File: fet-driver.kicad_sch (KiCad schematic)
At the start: 32 parts, among them Q21 AO3401, Q22 AO3401, Q23 AO3401, Q24 AO3401, Q25 AO3401, Q26 AO3401, Q27 AO3401, Q28 AO3401

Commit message: KiCAD ver. up
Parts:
- renumbered C47 to C39, C48 to C40, C49 to C41, C50 to C42, C51 to C43, C52 to C44, C53 to C45, C54 to C46, Q21 to Q13, Q22 to Q14, Q23 to Q15, Q24 to Q16, Q25 to Q17, Q26 to Q18, Q27 to Q19, Q28 to Q20, R90 to R66, R91 to R67, R92 to R68, R93 to R69, R94 to R70, R95 to R71, R96 to R72, R97 to R73, R106 to R82, R107 to R83, R108 to R84, R109 to R85, R110 to R86, R111 to R87, R112 to R88, R113 to R89

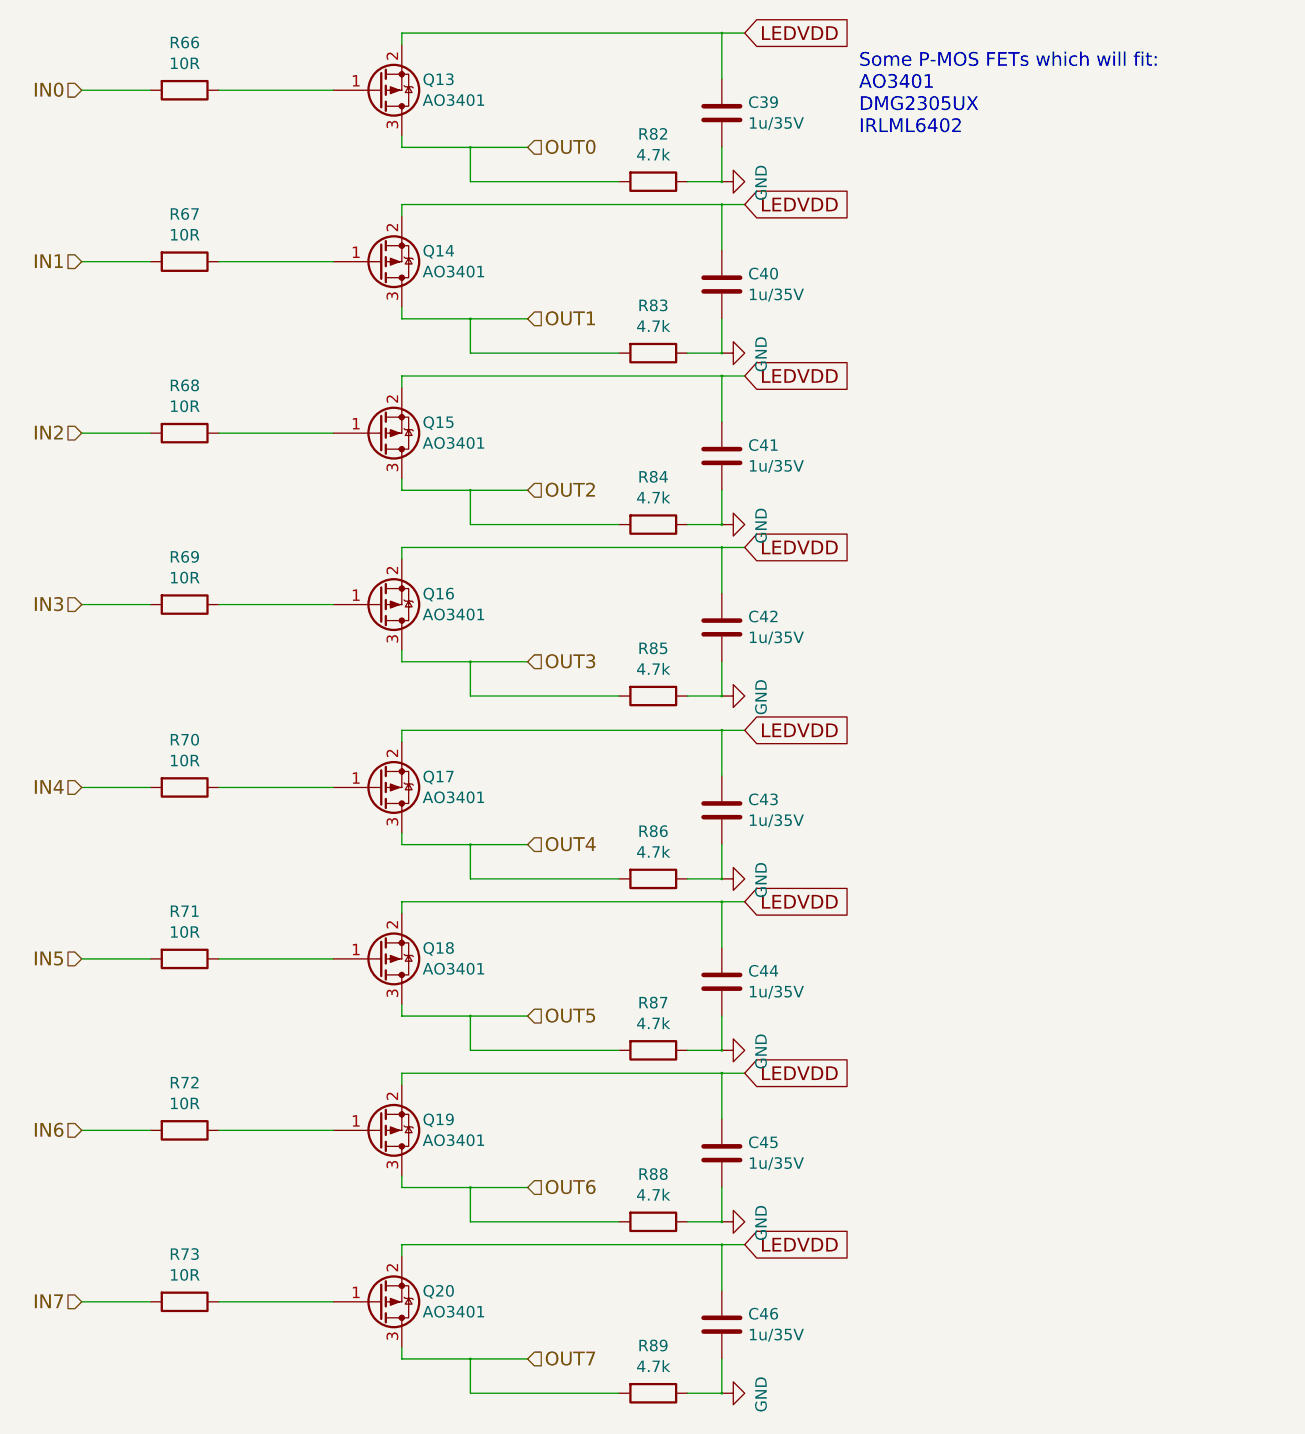
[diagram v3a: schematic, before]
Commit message: Added C94; Moved I2C pull-up Rs to more near MCU
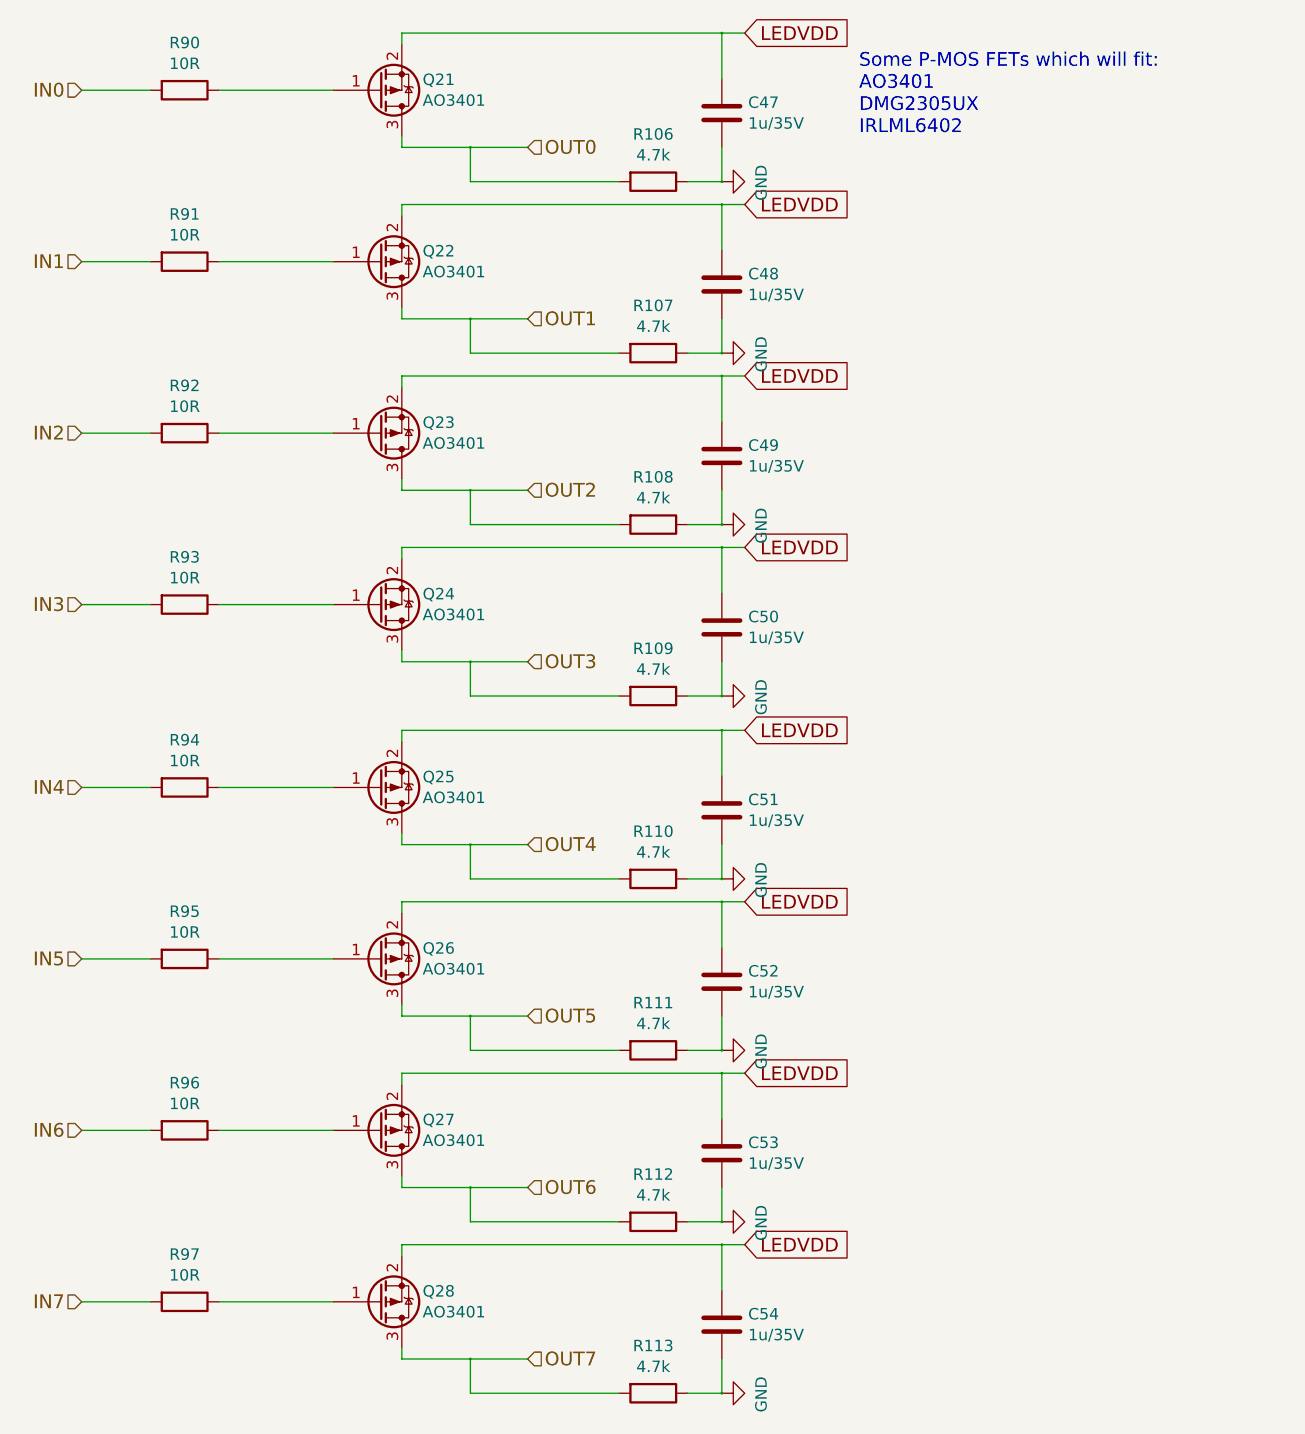
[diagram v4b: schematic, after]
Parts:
- renumbered C39 to C47, C40 to C48, C41 to C49, C42 to C50, C43 to C51, C44 to C52, C45 to C53, C46 to C54, Q13 to Q21, Q14 to Q22, Q15 to Q23, Q16 to Q24, Q17 to Q25, Q18 to Q26, Q19 to Q27, Q20 to Q28, R82 to R106, R83 to R107, R84 to R108, R85 to R109, R86 to R110, R87 to R111, R88 to R112, R89 to R113, R66 to R90, R67 to R91, R68 to R92, R69 to R93, R70 to R94, R71 to R95, R72 to R96, R73 to R97
